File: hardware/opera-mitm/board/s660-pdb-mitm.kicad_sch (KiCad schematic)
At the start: 89 parts, among them J1 JST B7B-XH-A, J101 MC 1,5/4-G-5.08, J102 MC 1,5/2-G-5.08, J103 Pi link 2x5, J104 ISP 2x3 DNP, J2 JST B3B-XH-A, K1 G6K-2F-Y 5VDC, K101 G2RL-1A DC12, Q1 2N7002, Q102 MMBT2222A, Q103 2N7002, Q2 2N7002, Q3 2N7002, Q4 2N7002, Q5 2N7002, SW101 TS-1187A-B-A-B, SW2 TS-1187A-B-A-B, U1 Raspberry Pi Pico 2 W, U101 ATtiny85-20SU, U102 LM2936MPX-3.3, U103 EL817S

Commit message: Buddy board rev B: Phoenix MC harness header, Pico socketed (DNP), labelled back silkscreen
J1 (car-harness OPERA lines) is now a Phoenix MC 1,5/7-G-5.08 pluggable header on the top
edge between J102 and J101, replacing the mid-board JST XH: the harness pigtail gets ferrules
and a MC 1,5/7-ST-5.08 plug, matching the power terminals. Same pin order (1 TXp ... 7 GND).
U102 (LM2936) with C105/C107 moved into the pocket the JST left, beside K1; its 12V feed,
3V3_AON output and the six J1 nets re-routed, RLY_COIL re-routed to clear the LDO pad.

U1 (Pico 2 W) is marked do-not-populate: the owner supplies the module and the board gets
two 1x20 female headers, listed in the hand-fit BOM. Mounting holes set to 4.0 mm from the
sides and 6.1 mm from top/bottom to match the TOFU.

Silkscreen: back-side labels name every wire at J101 (Constant/ACC/IG2/Ground, Honda option
coupler), J1 (panel pins, panel/HU side) and J102 (12V OUT/GND), plus a J103-to-Pi-GPIO
table; front carries the board title and LED legends.

Checks: DRC 0/0/0 with the Power12V (0.3 mm) and Supply net classes in force, schematic
parity 0, schematic-to-board netlist identical on all 262 pads, one GND net, ERC only the
known Pico-symbol GND/AGND artefact.

fab/rev-B replaces fab/rev-A (never ordered): Gerbers + drills (186 PTH = 90 THT pads + 96
vias, 4 NPTH), JLCPCB SMT BOM/CPL (72 parts, 27 line items, all with LCSC numbers), hand-fit
list, README with the upload steps and the mandatory placement-preview note.

COMBINED.md/DESIGN.md record the J1 change and the corrected Phoenix order number (1836231).

Co-Authored-By: Claude Fable 5.1 <noreply@anthropic.com>
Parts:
- J1: value JST B7B-XH-A -> MC 1,5/7-G-5.08; footprint Connector_JST:JST_XH_B7B-XH-A_1x07_P2.50mm_Vertical -> Connector_Phoenix_MC_HighVoltage:PhoenixContact_MC_1,5_7-G-5.08_1x07_P5.08mm_Horizontal; Fitting (none) -> Pluggable header, hand-fitted; mate with MC 1,5/7-ST-5.08 p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; LCSC C144398 -> (none); MPN B7B-XH-A -> MC 1,5/7-G-5.08 (1836231); Manufacturer JST -> Phoenix Contact
- U1: Fitting Socketed on 2x 1x20 female 2.54 mm headers, hand-fitted; no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 -> DNP – owner supplies the Pico 2 W. Fit two 1x20 2.54 mm sin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; now not fitted
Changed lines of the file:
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@@
 			)
 		)
-		(property "Value" "JST B7B-XH-A"
+		(property "Value" "MC 1,5/7-G-5.08"
 			(at 312.42 326.39 0)
 			(show_name no)
@@
 			)
 		)
-		(property "Footprint" "Connector_JST:JST_XH_B7B-XH-A_1x07_P2.50mm_Vertical"
+		(property "Footprint" "Connector_Phoenix_MC_HighVoltage:PhoenixContact_MC_1,5_7-G-5.08_1x07_P5.08mm_Horizontal"
 			(at 312.42 316.23 0)
 			(hide yes)
@@
 			)
 		)
-		(property "LCSC" "C144398"
+		(property "LCSC" ""
 			(at 312.42 316.23 0)
 			(hide yes)
@@
 			)
 		)
-		(property "MPN" "B7B-XH-A"
+		(property "MPN" "MC 1,5/7-G-5.08 (1836231)"
 			(at 312.42 316.23 0)
 			(hide yes)
@@
 			)
 		)
-		(property "Manufacturer" "JST"
+		(property "Manufacturer" "Phoenix Contact"
+			(at 312.42 316.23 0)
+			(hide yes)
+			(show_name no)
+			(do_not_autoplace no)
+			(effects
+				(font
+					(size 1.27 1.27)
+				)
+			)
+		)
+		(property "Fitting" "Pluggable header, hand-fitted; mate with MC 1,5/7-ST-5.08 plug, use ferrules on 16-18 AWG"
 			(at 312.42 316.23 0)
 			(hide yes)
@@
 		(on_board yes)
 		(in_pos_files yes)
-		(dnp no)
+		(dnp yes)
 		(property "Reference" "U1"
 			(at 400.05 154.94 0)
@@
 			)
 		)
-		(property "Fitting" "Socketed on 2x 1x20 female 2.54 mm headers, hand-fitted; not JLCPCB-assembled"
+		(property "Fitting" "DNP – owner supplies the Pico 2 W. Fit two 1x20 2.54 mm single-row FEMALE headers (Harwin M20-782 series or equivalent) in U1's pad rows."
 			(at 419.1 190.5 0)
 			(hide yes)

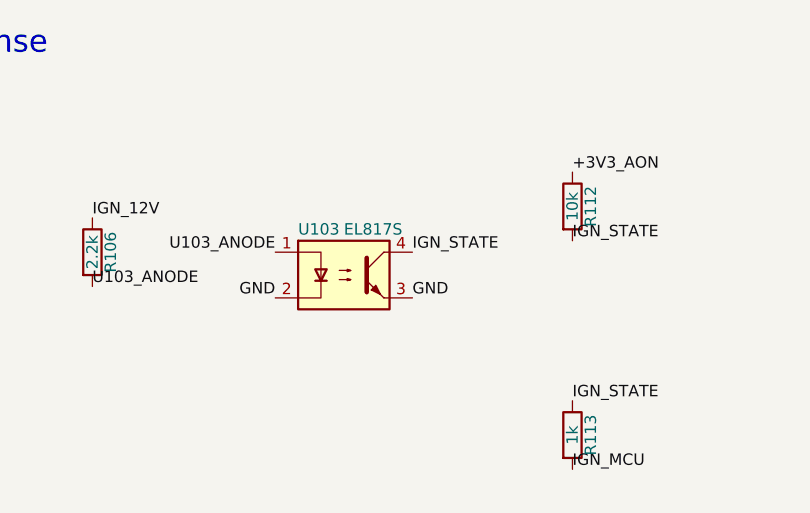
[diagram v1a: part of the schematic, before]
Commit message: U103: EL817S1 -> LTV-357T-B (C33068) to fit the SOP-4 2.54 mm footprint
JLCPCB flagged C63268 as not matching U103's footprint: the EL817S1 is a
gull-wing SMD DIP-4 (~10 mm lead span), the pads are 5.5 mm apart. The
Lite-On LTV-357T-B is a mini-flat SOP-4 with the same pinout. No copper change.

Co-Authored-By: Claude Opus 5.5 <noreply@anthropic.com>
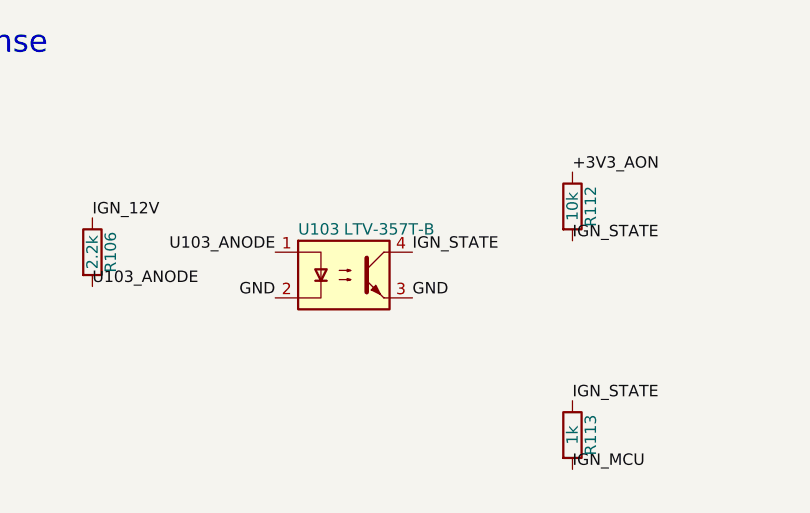
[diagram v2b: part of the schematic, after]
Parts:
- U103: value EL817S -> LTV-357T-B; LCSC C63268 -> C33068; MPN EL817S -> LTV-357T-B; Manufacturer Everlight -> Lite-On
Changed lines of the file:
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@@
 			)
 		)
-		(property "Value" "EL817S"
+		(property "Value" "LTV-357T-B"
 			(at 231.14 43.18 0)
 			(show_name no)
@@
 			)
 		)
-		(property "LCSC" "C63268"
+		(property "LCSC" "C33068"
 			(at 231.14 48.26 0)
 			(hide yes)
@@
 			)
 		)
-		(property "MPN" "EL817S"
+		(property "MPN" "LTV-357T-B"
 			(at 231.14 48.26 0)
 			(hide yes)
@@
 			)
 		)
-		(property "Manufacturer" "Everlight"
+		(property "Manufacturer" "Lite-On"
 			(at 231.14 48.26 0)
 			(hide yes)
